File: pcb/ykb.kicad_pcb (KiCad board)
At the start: 2 copper layers, 303.4 x 131.6 mm, 90 parts, among them SW1 Switch, U1 Helios

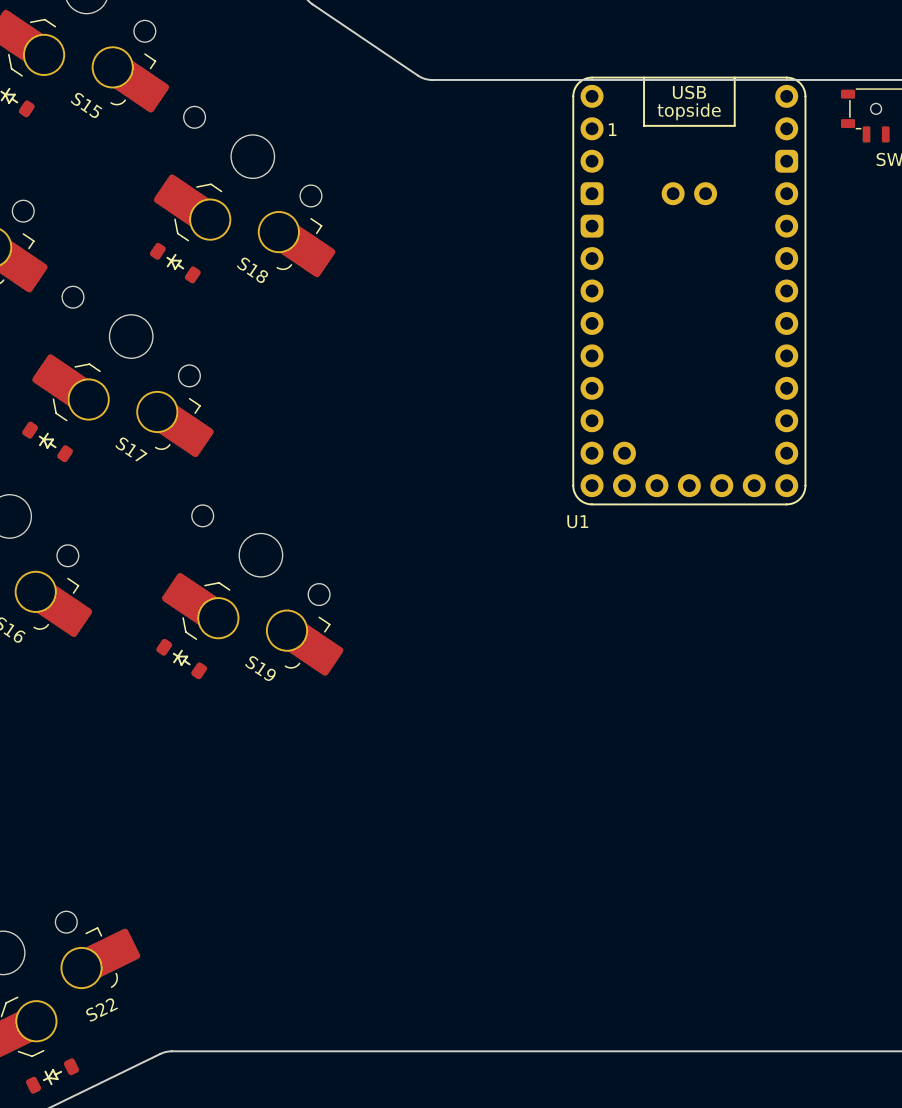
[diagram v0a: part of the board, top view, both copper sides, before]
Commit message: switched to castlated controller :3
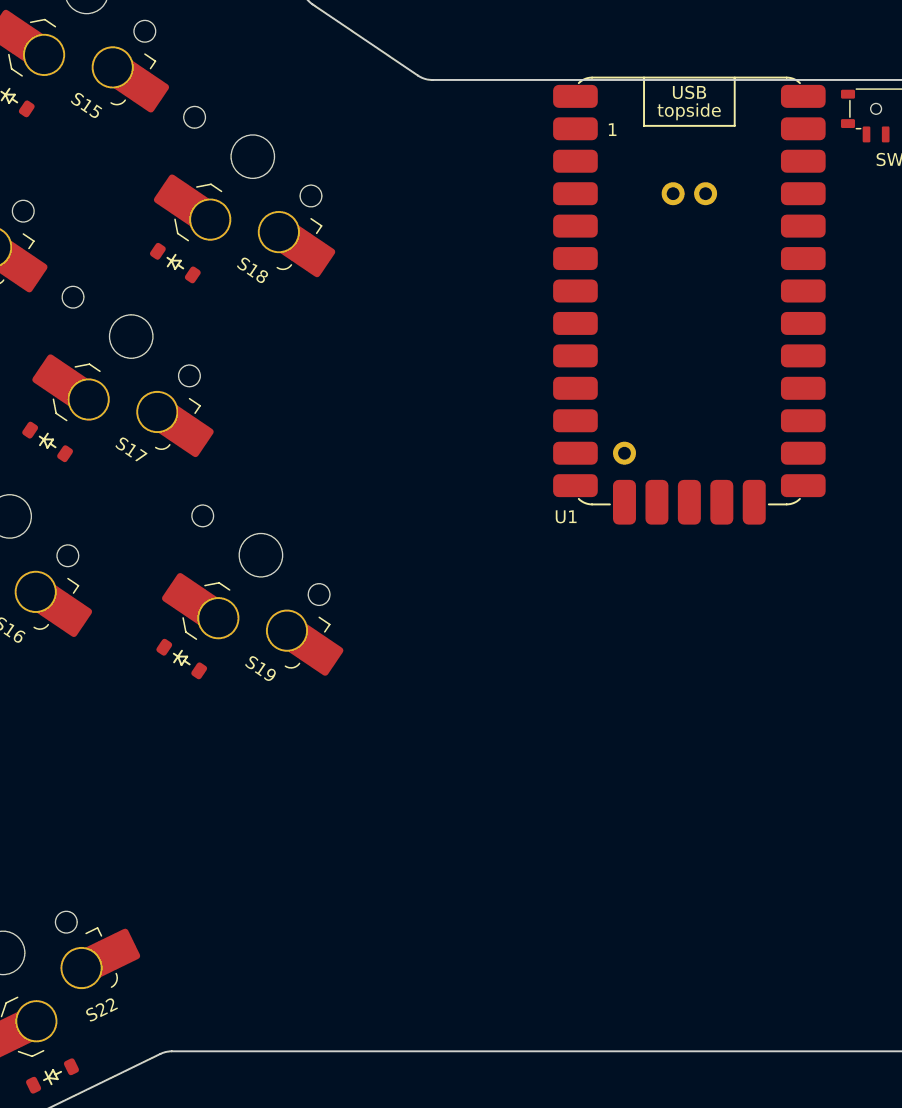
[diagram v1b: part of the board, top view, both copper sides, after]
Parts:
- U1: footprint PCM_marbastlib-xp-promicroish:Helios_AH_USBup -> PCM_marbastlib-xp-promicroish:Helios_AC
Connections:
- D10 pad 1: row 0 -> row 2
- D12 pad 1: row 2 -> row 0
- D13 pad 1: row 0 -> row 2
- D15 pad 1: row 2 -> row 0
- D16 pad 1: row 0 -> row 2
- D18 pad 1: row 2 -> row 0
- D7 pad 1: row 0 -> row 2
- D9 pad 1: row 2 -> row 0
- SW1 pad 1: unconnected-(SW1-Pad1) -> gnd
- SW1 pad 2: unconnected-(SW1-Pad2) -> rst
- U1 pad 10: unconnected-(U1-P7-Pad10) -> col 5
- U1 pad 11: unconnected-(U1-P8-Pad11) -> col 6
- U1 pad 12: unconnected-(U1-P9-Pad12) -> col 7
- U1 pad 14: unconnected-(U1-GND-Pad14) -> gnd
- U1 pad 15: unconnected-(U1-RST-Pad15) -> rst
- U1 pad 16: unconnected-(U1-3V3-Pad16) -> 3v3
- U1 pad 17: unconnected-(U1-P29-Pad17) -> row 3
- U1 pad 18: unconnected-(U1-P28-Pad18) -> row 2
- U1 pad 19: unconnected-(U1-P27-Pad19) -> row 1
- U1 pad 20: unconnected-(U1-P26-Pad20) -> row 0
- U1 pad 21: unconnected-(U1-P22-Pad21) -> col 13
- U1 pad 22: unconnected-(U1-P20-Pad22) -> col 12
- U1 pad 23: unconnected-(U1-P23-Pad23) -> col 11
- U1 pad 24: unconnected-(U1-P21-Pad24) -> col 10
- U1 pad 30: unconnected-(U1-P11-Pad30) -> col 9
- U1 pad 31: unconnected-(U1-P10-Pad31) -> col 8
- U1 pad 5: unconnected-(U1-P2-Pad5) -> col 0
- U1 pad 6: unconnected-(U1-P3-Pad6) -> col 1
- U1 pad 7: unconnected-(U1-P4-Pad7) -> col 2
- U1 pad 8: unconnected-(U1-P5-Pad8) -> col 3
- U1 pad 9: unconnected-(U1-P6-Pad9) -> col 4

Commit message: switched splay from key units to degrees because i did key units for some reason
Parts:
- removed SW1: Switch, ScottoKeebs_Components:Switch_MSK12C02
- S1, S10, S11, S12, S13, S14, S15, S16, S17, S18, S19, S2, S20, S21, S22, S23, S24, S25, S26, S27, S28, S29, S3, S30, S31, S32, S33, S34, S35, S36, S37, S38, S39, S4, S40, S41, S42, S43, S44, S5, S6, S7, S8, S9: footprint PCM_marbastlib-choc:SW_choc_v1_HS_CPG135001S30_1u -> ScottoKeebs_Hotswap:Hotswap_Choc_V1V2_1.00u
- moved S9 41.7 mm to (144.6, 114.0), turned to -26 degrees
- moved S18 41.5 mm to (192.7, 151.8), turned to -36 degrees
- moved S15 41.4 mm to (180.1, 138.4), turned to -36 degrees
- moved U1 41.1 mm to (225.1, 164.5)
- moved S12 41.0 mm to (166.1, 119.9), turned to -31 degrees
- moved S17 40.9 mm to (182.7, 165.5), turned to -36 degrees
- moved S14 40.9 mm to (170.1, 152.2), turned to -36 degrees
- moved S8 40.9 mm to (137.1, 129.2), turned to -26 degrees
- moved D9 40.8 mm to (142.4, 118.4), turned to -26 degrees
- moved S19 40.8 mm to (192.2, 183.0), turned to -36 degrees
- moved D12 40.8 mm to (163.6, 124.2), turned to -31 degrees
- moved D15 40.7 mm to (177.2, 142.5), turned to -36 degrees
- moved S11 40.6 mm to (157.4, 134.5), turned to -31 degrees
- moved D18 40.6 mm to (189.7, 155.8), turned to -36 degrees
- moved D17 40.4 mm to (179.7, 169.6), turned to -36 degrees
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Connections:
- D1 pad 1: row 2 -> Net-(D1-K)
- D10 pad 1: row 2 -> Net-(D1-K)
- D13 pad 1: row 2 -> Net-(D1-K)
- D16 pad 1: row 2 -> Net-(D1-K)
- D19 pad 1: row 2 -> row 3
- D4 pad 1: row 2 -> Net-(D1-K)
- D41 pad 1: row 2 -> row 3
- D7 pad 1: row 2 -> Net-(D1-K)
- S19 pad 1: col 6 -> col 5
- S20 pad 1: col 4 -> col 2
- S21 pad 1: col 5 -> col 3
- S22 pad 1: col 6 -> col 4
- S23 pad 1: col 13 -> col 11
- S24 pad 1: col 13 -> col 11
- S25 pad 1: col 13 -> col 11
- S26 pad 1: col 12 -> col 10
- S27 pad 1: col 12 -> col 10
- S28 pad 1: col 12 -> col 10
- S29 pad 1: col 11 -> col 9
- S30 pad 1: col 11 -> col 9
- S31 pad 1: col 11 -> col 9
- S32 pad 1: col 10 -> col 8
- S33 pad 1: col 10 -> col 8
- S34 pad 1: col 10 -> col 8
- S35 pad 1: col 9 -> col 7
- S36 pad 1: col 9 -> col 7
- S37 pad 1: col 9 -> col 7
- S38 pad 1: col 8 -> col 6
- S39 pad 1: col 8 -> col 6
- S40 pad 1: col 8 -> col 6
- S41 pad 1: col 7 -> col 6
- U1 pad 11: col 6 -> row 0
- U1 pad 12: col 7 -> row 1
- U1 pad 17: row 3 -> col 11
- U1 pad 18: row 2 -> col 10
- U1 pad 19: row 1 -> col 9
- U1 pad 20: row 0 -> col 8
- U1 pad 21: col 13 -> col 7
- U1 pad 22: col 12 -> col 6
- U1 pad 23: col 11 -> row 3
- U1 pad 24: col 10 -> row 2
- U1 pad 30: col 9 -> unconnected-(U1-P11-Pad30)
- U1 pad 31: col 8 -> unconnected-(U1-P10-Pad31)
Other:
- board size 303.4 x 131.6 mm -> 299.2 x 132.3 mm

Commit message: fixed cut
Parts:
- D1, D10, D11, D12, D13, D14, D15, D16, D17, D18, D19, D2, D20, D21, D22, D3, D4, D5, D6, D7, D8, D9: moved to B.Cu
- moved D5 9.07 mm to (119.5, 140.0), turned to 79 degrees
- moved D7 8.97 mm to (135.5, 153.0), turned to 64 degrees
- moved D12 8.84 mm to (171.0, 129.0), turned to 59 degrees
- moved D1 8.83 mm to (97.5, 158.0), turned to 84 degrees
- moved D15 8.80 mm to (184.0, 148.0), turned to 54 degrees
- moved D21 8.80 mm to (156.5, 206.0), turned to 39 degrees
- moved D4 8.78 mm to (116.0, 156.5), turned to 79 degrees
- moved D10 8.78 mm to (153.5, 158.0), turned to 59 degrees
- moved D6 8.76 mm to (122.5, 123.0), turned to 79 degrees
- moved D3 8.76 mm to (101.0, 124.0), turned to 84 degrees
- moved D8 8.70 mm to (142.5, 138.0), turned to 64 degrees
- moved D17 8.70 mm to (186.5, 175.0), turned to 54 degrees
- moved D14 8.64 mm to (174.0, 161.5), turned to 54 degrees
- moved D9 8.64 mm to (150.0, 122.5), turned to 64 degrees
- moved D20 8.61 mm to (142.5, 189.5), turned to 54 degrees
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
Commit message: fixed model refs, placed all diodes
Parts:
- added REF**: Standoff_M2x6mm, ScottoKeebs_Scotto:Standoff_M2x6mm, F.Cu at (200.0, 170.0)
- added REF**: Standoff_M2x6mm, ScottoKeebs_Scotto:Standoff_M2x6mm, F.Cu at (345.0, 165.0)
- added REF**: Standoff_M2x6mm, ScottoKeebs_Scotto:Standoff_M2x6mm, F.Cu at (250.0, 170.0)
- added REF**: Standoff_M2x6mm, ScottoKeebs_Scotto:Standoff_M2x6mm, F.Cu at (177.5, 125.0)
- added REF**: Standoff_M2x6mm, ScottoKeebs_Scotto:Standoff_M2x6mm, F.Cu at (205.0, 215.0)
- added REF**: Standoff_M2x6mm, ScottoKeebs_Scotto:Standoff_M2x6mm, F.Cu at (320.0, 115.0)
- added REF**: Standoff_M2x6mm, ScottoKeebs_Scotto:Standoff_M2x6mm, F.Cu at (245.0, 215.0)
- added REF**: Standoff_M2x6mm, ScottoKeebs_Scotto:Standoff_M2x6mm, F.Cu at (346.5, 120.0)
- added REF**: Standoff_M2x6mm, ScottoKeebs_Scotto:Standoff_M2x6mm, F.Cu at (170.0, 200.0)
- added REF**: Standoff_M2x6mm, ScottoKeebs_Scotto:Standoff_M2x6mm, F.Cu at (103.5, 120.0)
- added REF**: Standoff_M2x6mm, ScottoKeebs_Scotto:Standoff_M2x6mm, F.Cu at (280.0, 200.0)
- added REF**: Standoff_M2x6mm, ScottoKeebs_Scotto:Standoff_M2x6mm, F.Cu at (105.0, 165.0)
- added REF**: Standoff_M2x6mm, ScottoKeebs_Scotto:Standoff_M2x6mm, F.Cu at (130.0, 115.0)
- added REF**: Standoff_M2x6mm, ScottoKeebs_Scotto:Standoff_M2x6mm, F.Cu at (272.5, 125.0)
- D23, D24, D25, D26, D27, D28, D29, D30, D31, D32, D33, D34, D35, D36, D37, D38, D39, D40, D41, D42, D43, D44: moved to B.Cu
- moved D32 9.96 mm to (294.0, 153.5), turned to 121 degrees
- moved D39 9.47 mm to (266.0, 178.0), turned to 126 degrees
- moved D40 9.25 mm to (253.0, 161.5), turned to 126 degrees
- moved D41 9.06 mm to (253.5, 192.5), turned to 126 degrees
- moved D30 9.02 mm to (306.5, 136.5), turned to 116 degrees
- moved D27 8.86 mm to (330.7, 139.9), turned to 101 degrees
- moved D34 8.84 mm to (279.0, 129.0), turned to 121 degrees
- moved D23 8.83 mm to (352.5, 158.0), turned to 96 degrees
- moved D33 8.81 mm to (288.2, 144.1), turned to 121 degrees
- moved D37 8.80 mm to (266.0, 148.0), turned to 126 degrees
- moved D43 8.80 mm to (293.5, 206.0), turned to 141 degrees
- moved D35 8.79 mm to (286.0, 175.5), turned to 126 degrees
- moved D26 8.78 mm to (334.0, 156.5), turned to 101 degrees
- moved D29 8.77 mm to (315.0, 153.5), turned to 116 degrees
- moved D28 8.76 mm to (327.5, 123.0), turned to 101 degrees
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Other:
- outline, holes or cut-outs redrawn

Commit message: lcd footprint and started routing
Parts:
- removed REF** (x14): Standoff_M2x6mm, ScottoKeebs_Scotto:Standoff_M2x6mm
- added J1: Conn_01x08_Socket, Connector_PinHeader_2.54mm:PinHeader_1x08_P2.54mm_Vertical, F.Cu at (234.1, 187.5)
- moved D1 0.71 mm to (97.0, 158.5)
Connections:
- U1 pad 25: unconnected-(U1-P12-Pad25) -> DRST
- U1 pad 26: unconnected-(U1-P13-Pad26) -> DDC
- U1 pad 27: unconnected-(U1-P14-Pad27) -> DCS
- U1 pad 28: unconnected-(U1-P15-Pad28) -> DCLK
- U1 pad 29: unconnected-(U1-P16-Pad29) -> DDIN
- U1 pad 34: unconnected-(U1-P25-Pad34) -> DBL
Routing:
- net row 3: track 0.00 -> 135.9 mm
- net gnd: track 0.00 -> 41.4 mm, vias 0 -> 1
- net col 2: track 0.00 -> 36.0 mm
- net 3v3: track 0.00 -> 34.5 mm, vias 0 -> 1
- net col 1: track 0.00 -> 34.0 mm
- net col 5: track 0.00 -> 34.0 mm
- net col 4: track 0.00 -> 34.0 mm
- net col 0: track 0.00 -> 34.0 mm
- net col 3: track 0.00 -> 34.0 mm
- net DBL: track 0.00 -> 12.6 mm
- net Net-(D1-A): track 0.00 -> 7.89 mm
- net DCS: track 0.00 -> 7.76 mm, vias 0 -> 1
- net DDC: track 0.00 -> 7.73 mm, vias 0 -> 1
- net DRST: track 0.00 -> 7.71 mm, vias 0 -> 1
- net DDIN: track 0.00 -> 7.71 mm, vias 0 -> 1
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
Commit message: further routing
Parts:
- moved U1 12.7 mm to (237.4, 167.9)
- moved J1 12.5 mm to (246.3, 190.4)
- moved D11 12.3 mm to (174.1, 145.9)
- moved D13 12.3 mm to (175.9, 177.8)
- moved D1 12.2 mm to (109.0, 160.6)
- moved D14 12.2 mm to (185.9, 164.1)
- moved S38 12.2 mm to (289.2, 182.2)
- moved D29 12.2 mm to (326.8, 156.4)
- moved S14 12.2 mm to (181.9, 155.1)
- moved D25 12.2 mm to (361.3, 127.4)
- moved S3 12.2 mm to (104.6, 121.0)
- moved D24 12.2 mm to (362.8, 142.4)
- moved S26 12.2 mm to (353.4, 152.6)
- moved S15 12.2 mm to (191.9, 141.3)
- moved S17 12.2 mm to (194.5, 168.4)
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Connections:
- D1 pad 1: Net-(D1-K) -> row 2
- D4 pad 1: Net-(D1-K) -> row 2
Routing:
- net row 1: track 0.00 -> 453.6 mm, vias 0 -> 22
- net row 0: track 0.00 -> 369.2 mm, vias 0 -> 20
- net row 2: track 0.00 -> 365.3 mm, vias 0 -> 1
- net col 0: track 34.0 -> 233.2 mm, vias 0 -> 4
- net row 3: track 135.9 -> 288.8 mm, vias 0 -> 4
- net col 3: track 34.0 -> 173.2 mm, vias 0 -> 2
- net col 1: track 34.0 -> 158.4 mm
- net col 6: track 0.00 -> 121.8 mm
- net col 2: track 36.0 -> 146.2 mm
- net Net-(D1-K): track 0.00 -> 104.8 mm
- net col 5: track 34.0 -> 132.7 mm
- net col 11: track 0.00 -> 95.1 mm
- net col 10: track 0.00 -> 93.6 mm
- net col 9: track 0.00 -> 91.3 mm
- net col 8: track 0.00 -> 89.1 mm
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
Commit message: even more routing
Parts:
- moved D41 1.01 mm to (266.3, 195.6)
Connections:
- D10 pad 1: Net-(D1-K) -> row 2
- D13 pad 1: Net-(D1-K) -> row 2
- D16 pad 1: Net-(D1-K) -> row 2
- D7 pad 1: Net-(D1-K) -> row 2
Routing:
- net row 2: track 365.3 -> 704.6 mm, vias 1 -> 9
- net row 3: track 288.8 -> 554.3 mm, vias 4 -> 8
- net col 4: track 90.5 -> 278.8 mm, vias 0 -> 5
- net row 1: track 453.6 -> 566.1 mm, vias 22 -> 27
- net Net-(D1-K): track 104.8 -> 0.00 mm
- net col 5: track 132.7 -> 224.3 mm, vias 0 -> 4
- net col 1: track 158.4 -> 240.7 mm, vias 0 -> 2
- net col 2: track 146.2 -> 226.4 mm, vias 0 -> 2
- net col 3: track 173.2 -> 236.1 mm, vias 2 -> 4
- net row 0: track 369.2 -> 310.3 mm
- net col 0: track 233.2 -> 285.4 mm, vias 4 -> 6
- net Net-(D41-A): track 27.9 -> 31.0 mm
- net gnd: track 41.4 -> 39.9 mm

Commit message: reset row-controller routing, centered things better
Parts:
- moved J1 0.58 mm to (245.7, 190.4)
- moved U1 0.58 mm to (236.9, 167.9)
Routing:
- net row 2: track 704.6 -> 228.2 mm, vias 9 -> 3
- net col 0: track 285.4 -> 95.2 mm, vias 6 -> 0
- net col 4: track 278.8 -> 90.5 mm, vias 5 -> 0
- net row 3: track 554.3 -> 395.1 mm, vias 8 -> 4
- net col 1: track 240.7 -> 97.9 mm, vias 2 -> 0
- net col 3: track 236.1 -> 94.4 mm, vias 4 -> 0
- net col 5: track 224.3 -> 86.8 mm, vias 4 -> 0
- net col 2: track 226.4 -> 96.7 mm, vias 2 -> 0
- net row 1: track 566.1 -> 437.9 mm, vias 27 -> 23
- net Net-(D42-A): track 21.7 -> 0.00 mm
- net (no net): track 21.7 -> 0.00 mm
- net Net-(D43-A): track 22.2 -> 0.65 mm
- net Net-(D44-A): track 21.6 -> 0.67 mm
- net Net-(D21-A): track 7.78 -> 0.00 mm
- net Net-(D22-A): track 7.68 -> 0.00 mm
